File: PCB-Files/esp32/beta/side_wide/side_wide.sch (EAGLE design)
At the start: 11 parts

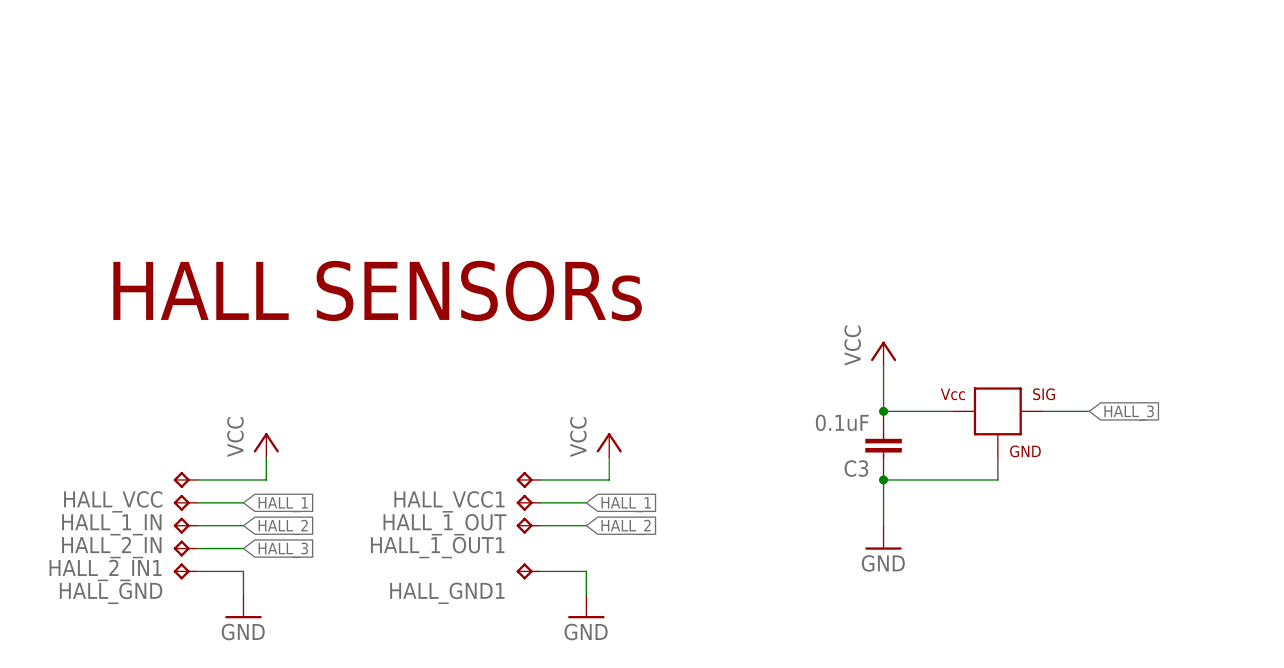
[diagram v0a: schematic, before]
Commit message: creates final PCB version; revised beta side pcbs to match beta main pcb pinouts
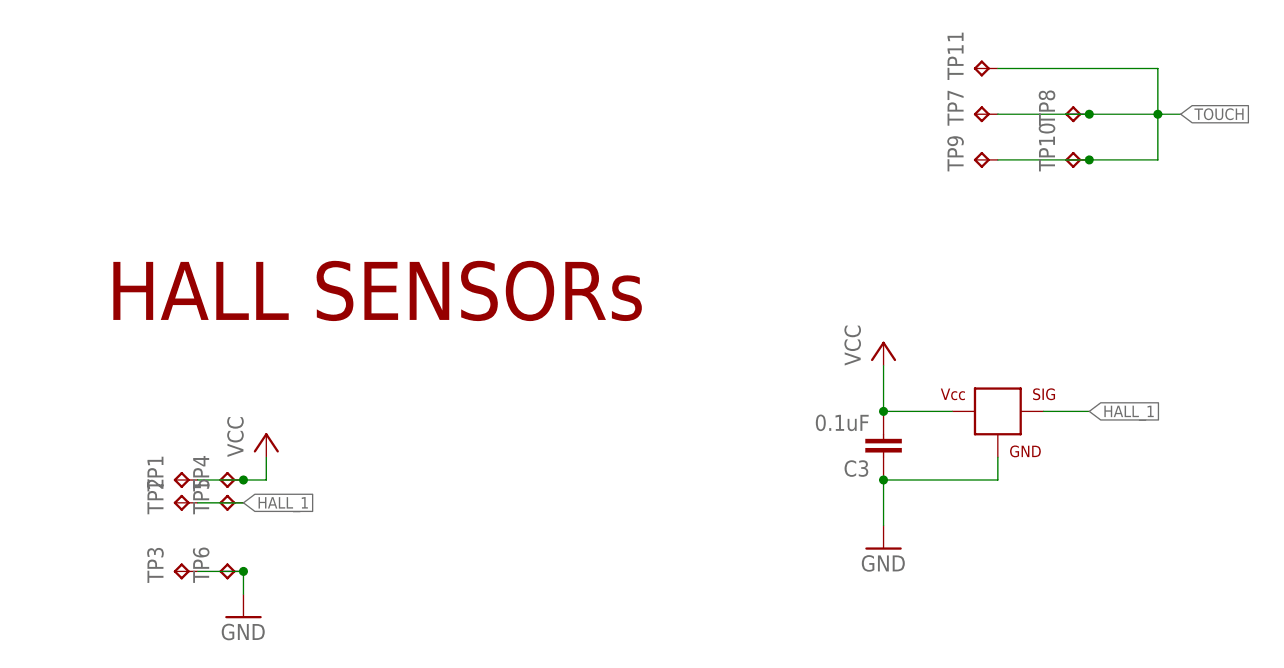
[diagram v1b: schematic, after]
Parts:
- removed HALL_1_IN, HALL_1_OUT, HALL_1_OUT1, HALL_2_IN, HALL_2_IN1, HALL_GND, HALL_GND1, HALL_VCC, HALL_VCC1: TPTP20SQ, testpad:TPTP20SQ
- added TP1, TP10, TP11, TP2, TP3, TP4, TP5, TP6, TP7, TP8, TP9: TPTP10SQ, testpad:TPTP10SQ
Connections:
- removed net HALL_2: HALL_1_OUT1.TP, HALL_2_IN.TP
- removed net HALL_3: HALL.SIG, HALL_2_IN1.TP
- new net TOUCH: TP10.TP, TP11.TP, TP7.TP, TP8.TP, TP9.TP
- net GND: now also TP3.TP, TP6.TP; no longer HALL_GND.TP, HALL_GND1.TP
- net HALL_1: now also HALL.SIG, TP2.TP, TP5.TP; no longer HALL_1_IN.TP, HALL_1_OUT.TP
- net VCC: now also TP1.TP, TP4.TP; no longer HALL_VCC.TP, HALL_VCC1.TP
